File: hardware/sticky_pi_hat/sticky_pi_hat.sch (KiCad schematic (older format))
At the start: 39 parts, among them J1 Screw_Terminal_01x11, J2 Conn_02x13_Odd_Even, J3 Conn_01x02_Male, Q1 BSS806NH6327XTSA1, Q2 AO3415A, Q3 BSS806NH6327XTSA1, Q4 BSS806NH6327XTSA1, SW1 SW_Push, U1 DHT22, U2 TPL5110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

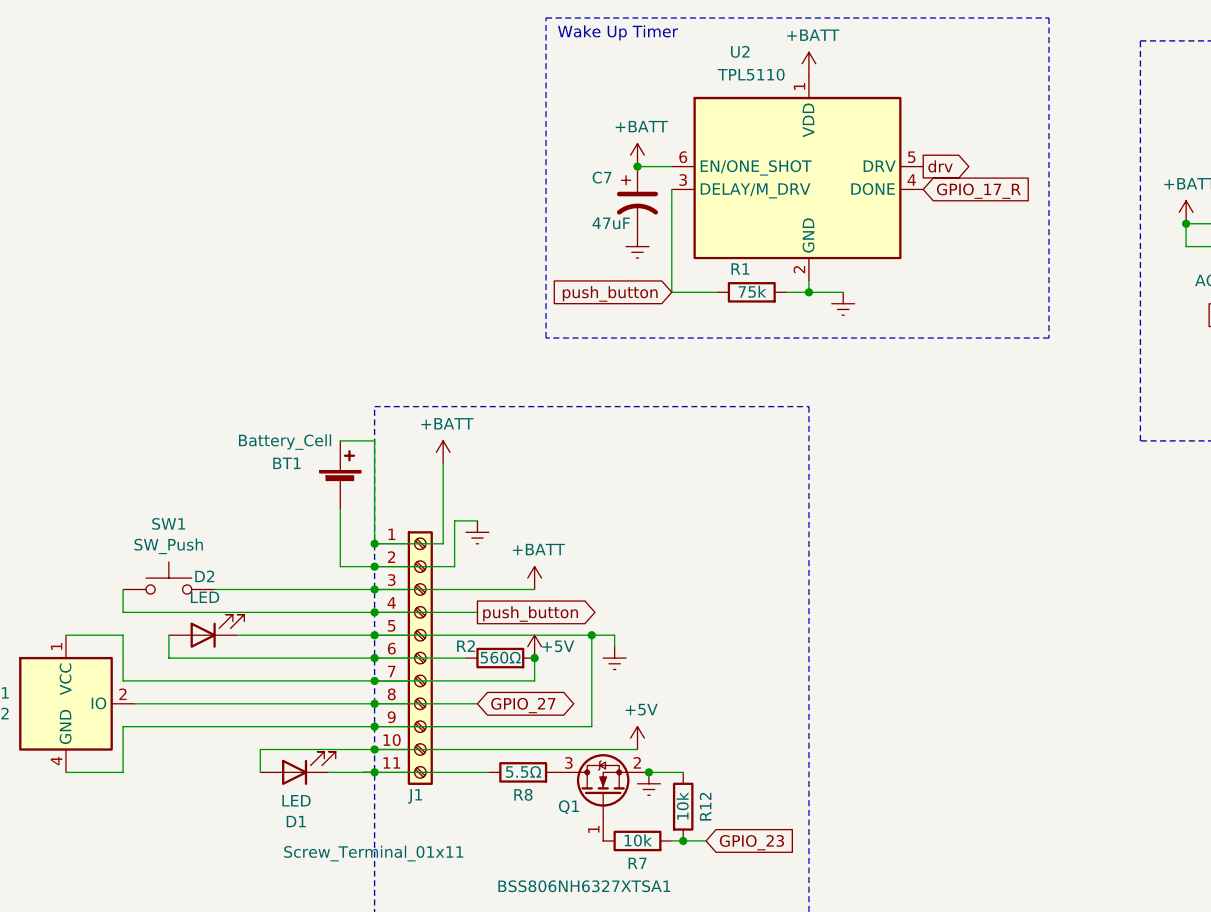
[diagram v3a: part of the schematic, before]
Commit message: add diode to prevent wrong measurement of R1(timing) dut to pushbutton state holder
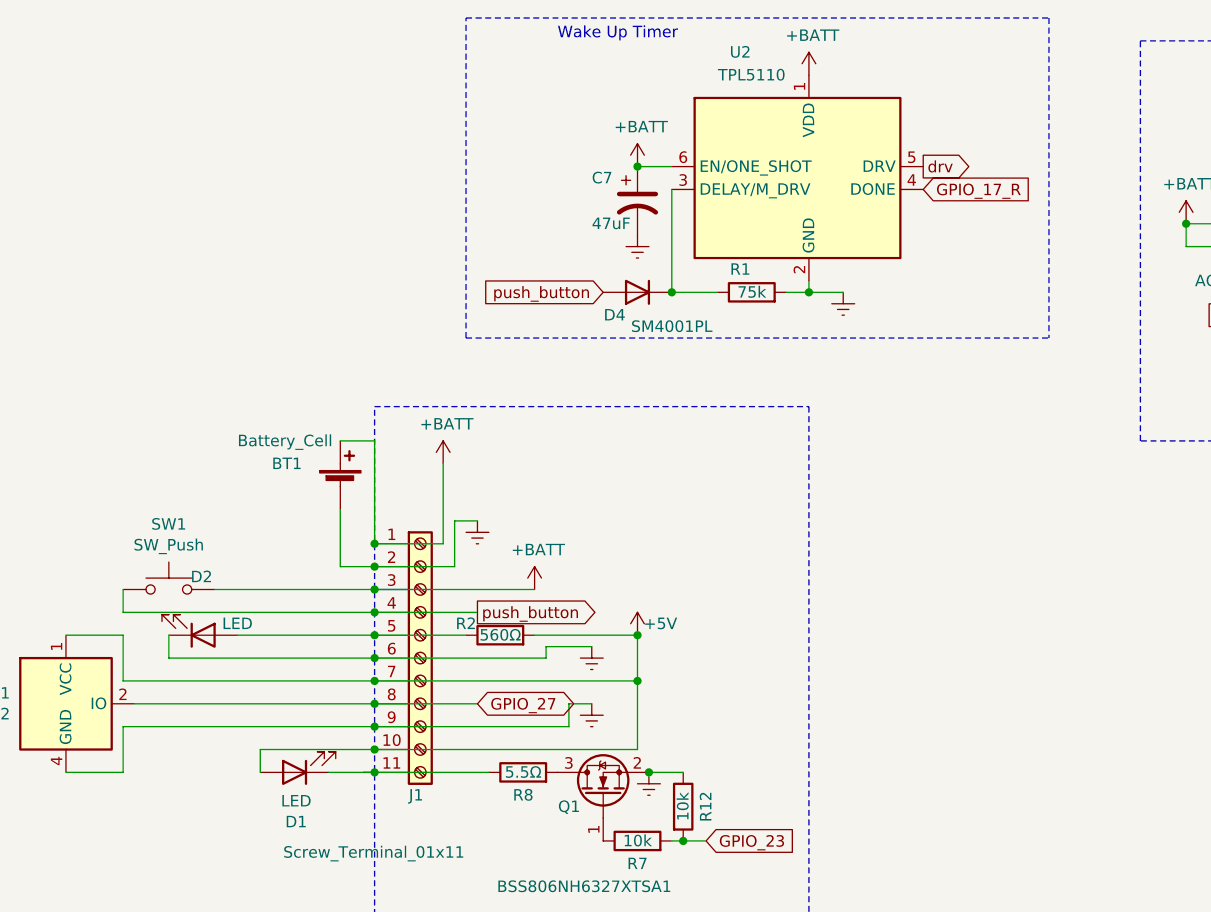
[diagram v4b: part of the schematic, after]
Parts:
- added D4: SM4001PL, Diode_SMD:D_SOD-123F, symbol Diode:SM4001
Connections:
- wire segments 117 -> 120
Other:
- moved on the sheet: D2, R2
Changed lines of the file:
@@
 	1    0    0    -1
-$EndComp
-$Comp
-L Device:LED D2
-U 1 1 6145E678
-P 2250 3400
-F 0 "D2" H 2243 3145 50  0000 C CNN
-F 1 "LED" H 2243 3236 50  0000 C CNN
-F 2 "#none" H 2250 3400 50  0001 C CNN
-F 3 "https://www.kingbrightusa.com/images/catalog/SPEC/WP7113SECK-J3.pdf" H 2250 3400 50  0001 C CNN
-F 4 "WP7113SECK/J3" H 2250 3400 50  0001 C CNN "part_number"
-F 5 "#none" H 2250 3400 50  0001 C CNN "Manufacturer"
-F 6 "WP7113SECK/J3" H 2250 3400 50  0001 C CNN "Part"
-	1    2250 3400
-	-1   0    0    1
 $EndComp
 Wire Wire Line
@@
 L Device:R R2
 U 1 1 6146BE2F
-P 3550 3500
-F 0 "R2" V 3600 3650 50  0000 C CNN
-F 1 "560Ω" V 3550 3500 50  0000 C CNN
-F 2 "Resistor_SMD:R_2010_5025Metric" V 3480 3500 50  0001 C CNN
-F 3 "https://www.yageo.com/upload/media/product/productsearch/datasheet/rchip/PYu-AC_51_RoHS_L_7.pdf" H 3550 3500 50  0001 C CNN
-F 4 "AC2010JK-07560RL" H 3550 3500 50  0001 C CNN "part_number"
-F 5 "YAGEO" H 3550 3500 50  0001 C CNN "Manufacturer"
-F 6 "" H 3550 3500 50  0001 C CNN "Vendor"
-F 7 "AC2010JK-07560RL" H 3550 3500 50  0001 C CNN "Part"
-	1    3550 3500
+P 3550 3400
+F 0 "R2" V 3600 3550 50  0000 C CNN
+F 1 "560Ω" V 3550 3400 50  0000 C CNN
+F 2 "Resistor_SMD:R_2010_5025Metric" V 3480 3400 50  0001 C CNN
+F 3 "https://www.yageo.com/upload/media/product/productsearch/datasheet/rchip/PYu-AC_51_RoHS_L_7.pdf" H 3550 3400 50  0001 C CNN
+F 4 "AC2010JK-07560RL" H 3550 3400 50  0001 C CNN "part_number"
+F 5 "YAGEO" H 3550 3400 50  0001 C CNN "Manufacturer"
+F 6 "" H 3550 3400 50  0001 C CNN "Vendor"
+F 7 "AC2010JK-07560RL" H 3550 3400 50  0001 C CNN "Part"
+	1    3550 3400
 	0    -1   -1   0
 $EndComp
@@
 	8200 4400 8300 4400
 $Comp
-L power:+5V #PWR0116
-U 1 1 613E357C
-P 4150 3900
-F 0 "#PWR0116" H 4150 3750 50  0001 C CNN
-F 1 "+5V" H 4165 4073 50  0000 C CNN
-F 2 "" H 4150 3900 50  0001 C CNN
-F 3 "" H 4150 3900 50  0001 C CNN
-	1    4150 3900
-	1    0    0    -1
-$EndComp
-$Comp
 L power:+5V #PWR0118
 U 1 1 613FA3A6
-P 3700 3500
-F 0 "#PWR0118" H 3700 3350 50  0001 C CNN
-F 1 "+5V" H 3800 3550 50  0000 C CNN
-F 2 "" H 3700 3500 50  0001 C CNN
-F 3 "" H 3700 3500 50  0001 C CNN
-	1    3700 3500
+P 4150 3400
+F 0 "#PWR0118" H 4150 3250 50  0001 C CNN
+F 1 "+5V" H 4250 3450 50  0000 C CNN
+F 2 "" H 4150 3400 50  0001 C CNN
+F 3 "" H 4150 3400 50  0001 C CNN
+	1    4150 3400
 	1    0    0    -1
 $EndComp
@@
 $EndComp
 Wire Wire Line
-	3400 3500 3000 3500
-Connection ~ 3000 3500
-Wire Wire Line
 	6300 5450 6300 5350
 $Comp
@@
 L power:Earth #PWR0122
 U 1 1 617550CA
-P 4050 3450
-F 0 "#PWR0122" H 4050 3200 50  0001 C CNN
-F 1 "Earth" H 4050 3300 50  0001 C CNN
-F 2 "" H 4050 3450 50  0001 C CNN
-F 3 "~" H 4050 3450 50  0001 C CNN
-	1    4050 3450
-	1    0    0    -1
-$EndComp
-Connection ~ 3000 3400
-Wire Wire Line
-	3000 3400 3950 3400
-Wire Wire Line
-	4050 3450 4050 3400
+P 3950 3700
+F 0 "#PWR0122" H 3950 3450 50  0001 C CNN
+F 1 "Earth" H 3950 3550 50  0001 C CNN
+F 2 "" H 3950 3700 50  0001 C CNN
+F 3 "~" H 3950 3700 50  0001 C CNN
+	1    3950 3700
+	1    0    0    -1
+$EndComp
 Connection ~ 4900 1900
 Wire Wire Line
@@
 	3000 3700 3450 3700
 Connection ~ 3000 3700
-Connection ~ 3000 3800
 $Comp
 L Transistor_FET:BSS123 Q1
@@
 Text GLabel 5400 1450 2    50   Input ~ 0
 GPIO_17_R
-Wire Wire Line
-	3700 3500 3700 3600
-Connection ~ 3700 3500
-Wire Wire Line
-	3700 3600 3000 3600
-Wire Wire Line
-	3950 3800 3950 3400
-Wire Wire Line
-	3000 3800 3950 3800
-Connection ~ 3950 3400
-Wire Wire Line
-	3950 3400 4050 3400
 $Comp
 L Device:R R6
@@
 Text Notes 4600 5950 0    50   ~ 0
 Battery Level ADC Reader
-Text GLabel 4300 1900 0    50   Input ~ 0
+Text GLabel 4000 1900 0    50   Input ~ 0
 push_button
 $Comp
@@
 Wire Notes Line
 	5950 700  5950 2100
-Wire Notes Line
-	5950 2100 3750 2100
-Wire Notes Line
-	3750 2100 3750 700
-Wire Notes Line
-	3750 700  5950 700
 Text Notes 5500 4850 0    50   ~ 0
 Button State Holder
@@
 Wire Wire Line
 	2100 6400 1800 6400
+$Comp
+L Device:LED D2
+U 1 1 6145E678
+P 2250 3400
+F 0 "D2" H 2243 3145 50  0000 C CNN
+F 1 "LED" H 2400 3350 50  0000 C CNN
+F 2 "#none" H 2250 3400 50  0001 C CNN
+F 3 "https://www.kingbrightusa.com/images/catalog/SPEC/WP7113SECK-J3.pdf" H 2250 3400 50  0001 C CNN
+F 4 "WP7113SECK/J3" H 2250 3400 50  0001 C CNN "part_number"
+F 5 "#none" H 2250 3400 50  0001 C CNN "Manufacturer"
+F 6 "WP7113SECK/J3" H 2250 3400 50  0001 C CNN "Part"
+	1    2250 3400
+	1    0    0    1
+$EndComp
+Wire Wire Line
+	3000 3400 3400 3400
+Connection ~ 3000 3400
+Wire Wire Line
+	3700 3400 4150 3400
+Connection ~ 4150 3400
+Wire Wire Line
+	4150 3900 4150 3600
+Connection ~ 4150 3600
+Wire Wire Line
+	4150 3600 4150 3400
+Wire Wire Line
+	3000 3600 4150 3600
+$Comp
+L power:Earth #PWR0116
+U 1 1 61C1218D
+P 3950 3450
+F 0 "#PWR0116" H 3950 3200 50  0001 C CNN
+F 1 "Earth" H 3950 3300 50  0001 C CNN
+F 2 "" H 3950 3450 50  0001 C CNN
+F 3 "~" H 3950 3450 50  0001 C CNN
+	1    3950 3450
+	1    0    0    -1
+$EndComp
+Wire Wire Line
+	3000 3500 3750 3500
+Wire Wire Line
+	3750 3500 3750 3450
+Wire Wire Line
+	3750 3450 3950 3450
+Connection ~ 3000 3500
+Wire Wire Line
+	3000 3800 3850 3800
+Wire Wire Line
+	3850 3800 3850 3700
+Wire Wire Line
+	3850 3700 3950 3700
+Connection ~ 3000 3800
+$Comp
+L Diode:SM4001 D4
+U 1 1 61D22407
+P 4150 1900
+F 0 "D4" H 4250 2000 50  0000 C CNN
+F 1 "SM4001PL" H 4000 2050 50  0000 C CNN
+F 2 "Diode_SMD:D_SOD-123F" H 4150 1725 50  0001 C CNN
+F 3 "http://cdn-reichelt.de/documents/datenblatt/A400/SMD1N400%23DIO.pdf" H 4150 1900 50  0001 C CNN
+F 4 "Micro Commercial Co" H 4150 1900 50  0001 C CNN "Manufacturer"
+F 5 "SM4001PL" H 4150 1900 50  0001 C CNN "Part"
+F 6 "SM4001PL" H 4150 1900 50  0001 C CNN "part_number"
+	1    4150 1900
+	-1   0    0    1
+$EndComp
+Connection ~ 4300 1900
+Wire Notes Line
+	3400 2100 3400 700
+Wire Notes Line
+	3400 700  5950 700
+Wire Notes Line
+	3400 2100 5950 2100
 $EndSCHEMATC
